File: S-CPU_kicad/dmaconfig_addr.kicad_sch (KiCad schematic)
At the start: 116 parts

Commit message: Big update on the hierarchical sheet. DMA section update too.
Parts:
- removed OCLC, OCLX: DFFR_A, symbol Ricoh_Cells:DFFR_A
- removed OMRS: INVERTER_A, symbol Ricoh_Cells:INVERTER_A
- removed ZOOJ: DFFR_B, symbol Ricoh_Cells:DFFR_B
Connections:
- net BUS_DIRECTION_FLAG: now reaches QKAG6.4 (Q)
- net wQKAG5 renamed INDIRECT_HDMA_FLAG
- net wWOVT renamed CYCLE_COUNTER0
- net wWOWE renamed CYCLE_COUNTER1
- no-connect marks 13 -> 9
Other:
- note removed: "DMA RW signal based on bus direction"
- moved on the sheet: DSAC, DSAZ, DSCS, DSKP, DSLL, DSSG, DSSX, DSWN, DSXY, DSYT, DSZC, OKWN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

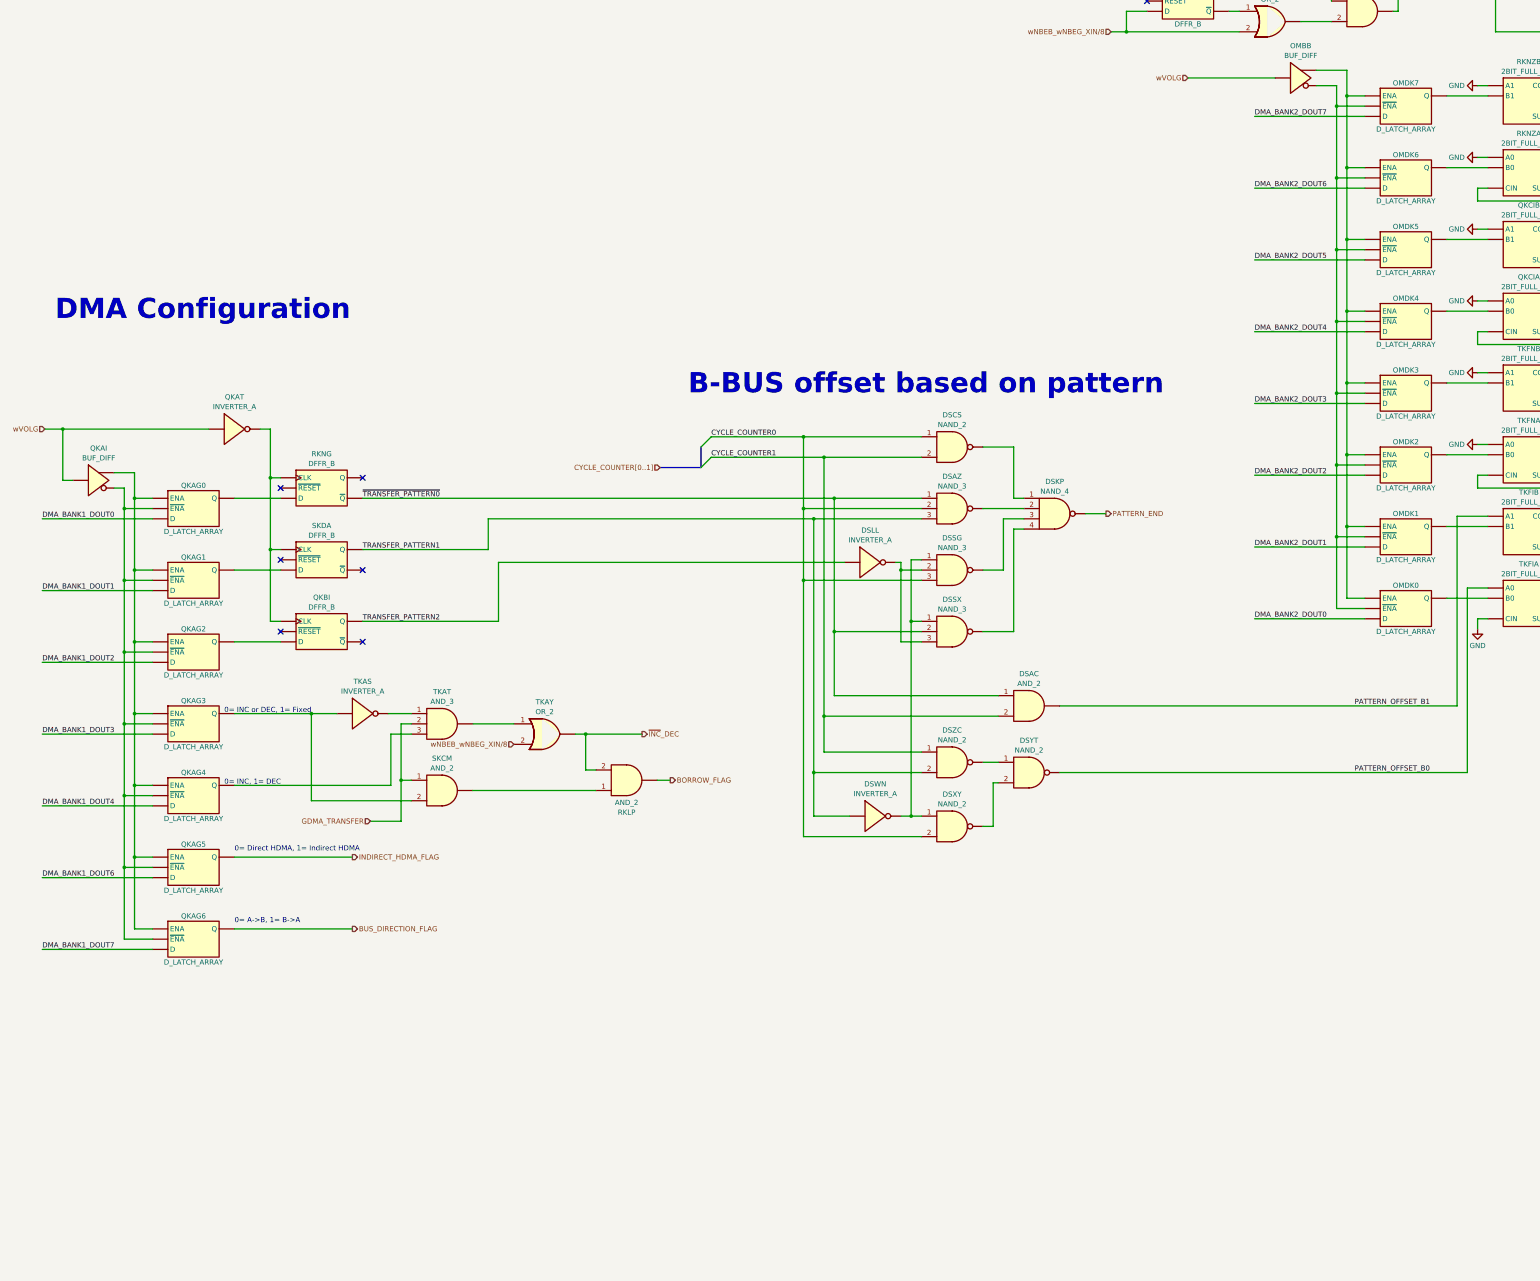
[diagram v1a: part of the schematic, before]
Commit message: DMA section update. Fixed gate related to INC/DEC and BORROW/CARRY FLAG
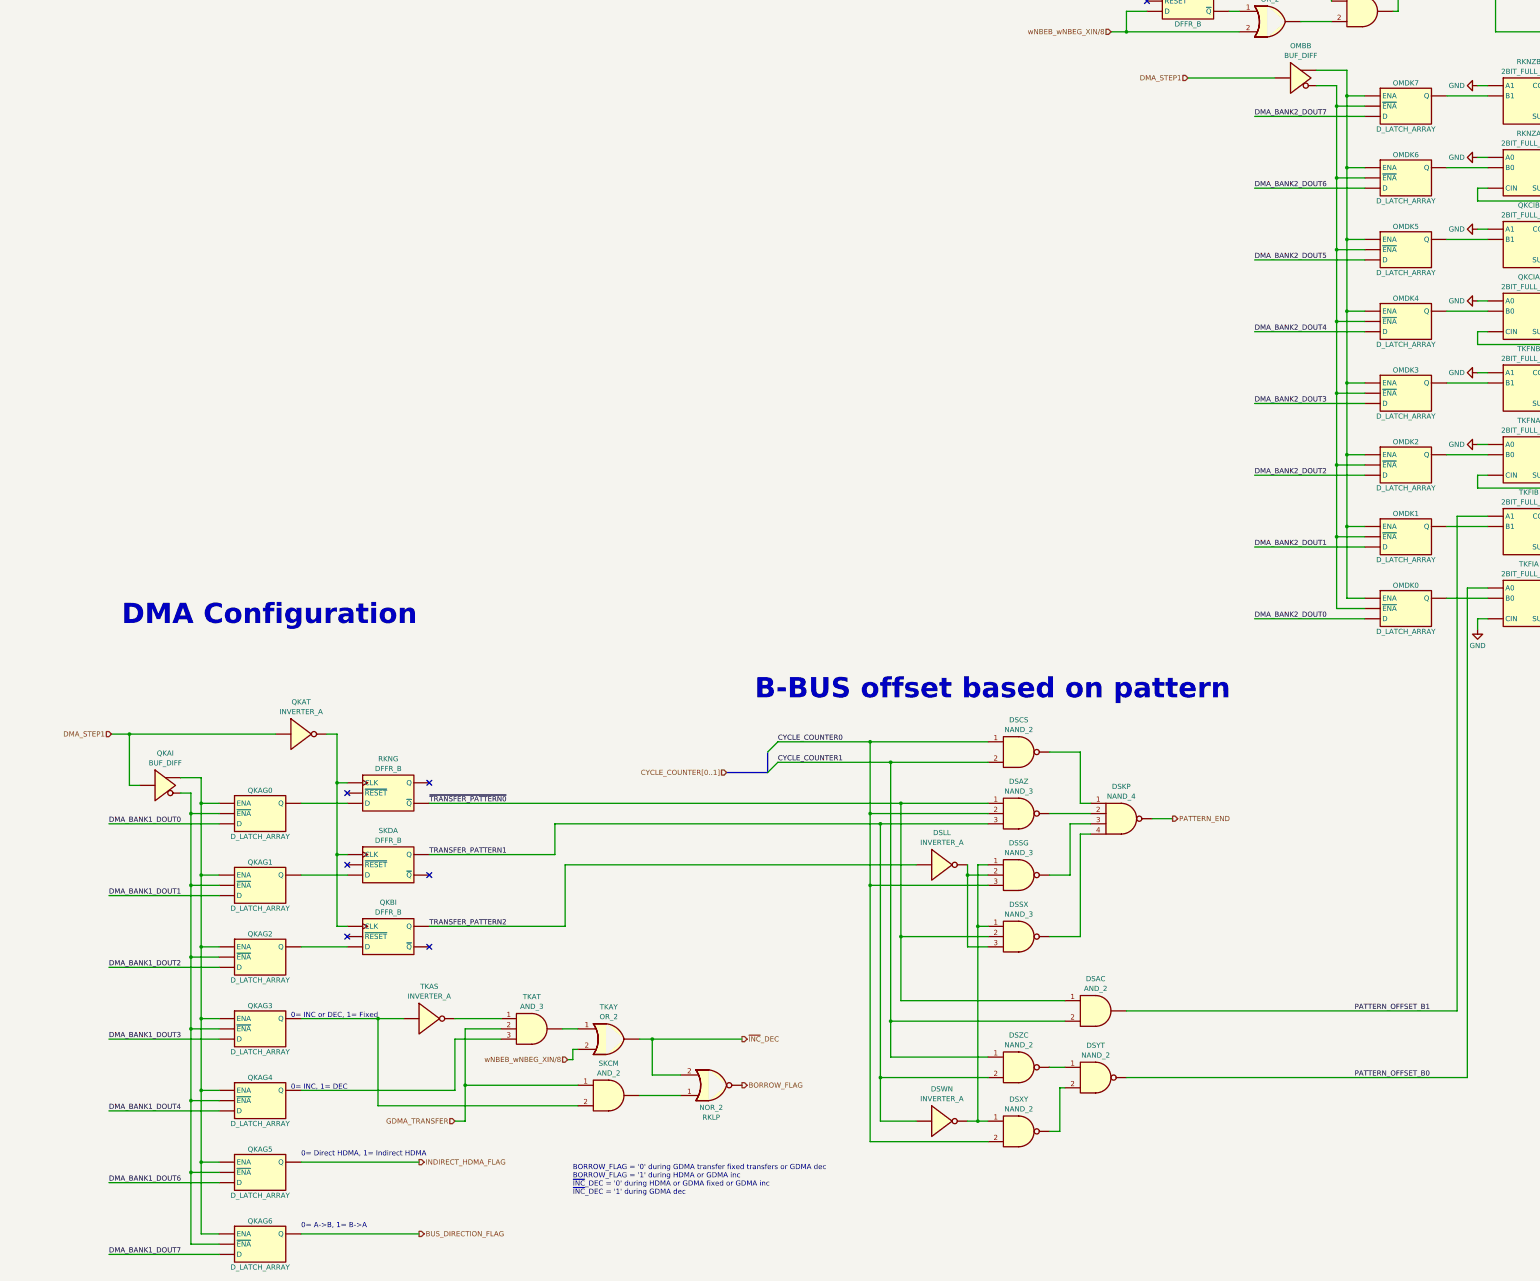
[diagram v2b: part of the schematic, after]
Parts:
- RKLP: value AND_2 -> NOR_2; symbol Ricoh_Cells:AND_2 -> Ricoh_Cells:NOR_2
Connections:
- net wVOLG renamed DMA_STEP1
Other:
- note added: "BORROW_FLAG = '0' during GDMA transfer fixed transfers or GDMA dec BORROW_FLAG = '1' during HDMA or GDMA inc ~{INC}_DEC = '0' during HDMA or GDMA fixed or GDMA inc ~{INC}_DEC = '1' during GDMA dec"
- moved on the sheet: DSAC, DSAZ, DSCS, DSKP, DSLL, DSSG, DSSX, DSWN, DSXY, DSYT, DSZC, QKAG0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

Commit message: DMA section update. Found errors between some MUX and MUXI gates.
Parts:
- TKHG: symbol Ricoh_Cells:OR_2 -> Ricoh_Cells:NOR_2
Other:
- note added: "LATCH_NEXT_DMA_ADDR_BUS is only valid for 1 mclk cycle every 8 cycles"
- note added: "Positive pulse on falling edge"
- moved on the sheet: SKKT, SKPA, TKGB, TKIB

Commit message: General update a
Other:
- note added: "LATCH_NEXT_DMA_ADDR_BUS is only valid for 1 mclk cycle every 8 cycles (on cycle 1)"
- note removed: "LATCH_NEXT_DMA_ADDR_BUS is only valid for 1 mclk cycle every 8 cycles"
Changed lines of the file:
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@@
     (effects (font (size 1.27 1.27)) (justify left bottom))
   )
-  (text "LATCH_NEXT_DMA_ADDR_BUS is only valid for 1 mclk cycle every 8 cycles"
+  (text "LATCH_NEXT_DMA_ADDR_BUS is only valid for 1 mclk cycle every 8 cycles (on cycle 1)"
     (at 425.45 57.15 0)
     (effects (font (size 1.27 1.27)) (justify left bottom))

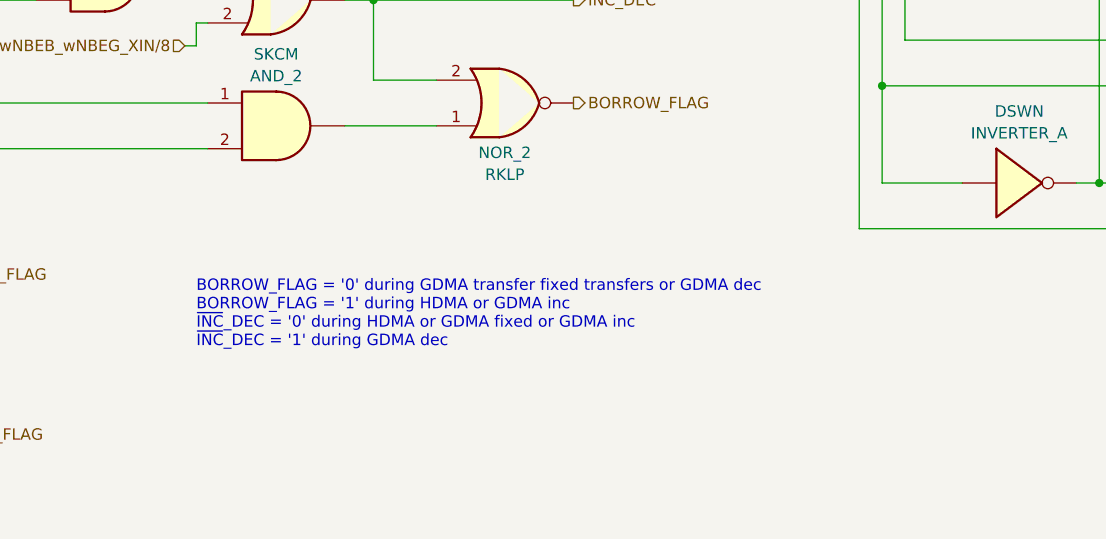
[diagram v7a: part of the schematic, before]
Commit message: More DMA updates - extra notes regarding behaviour
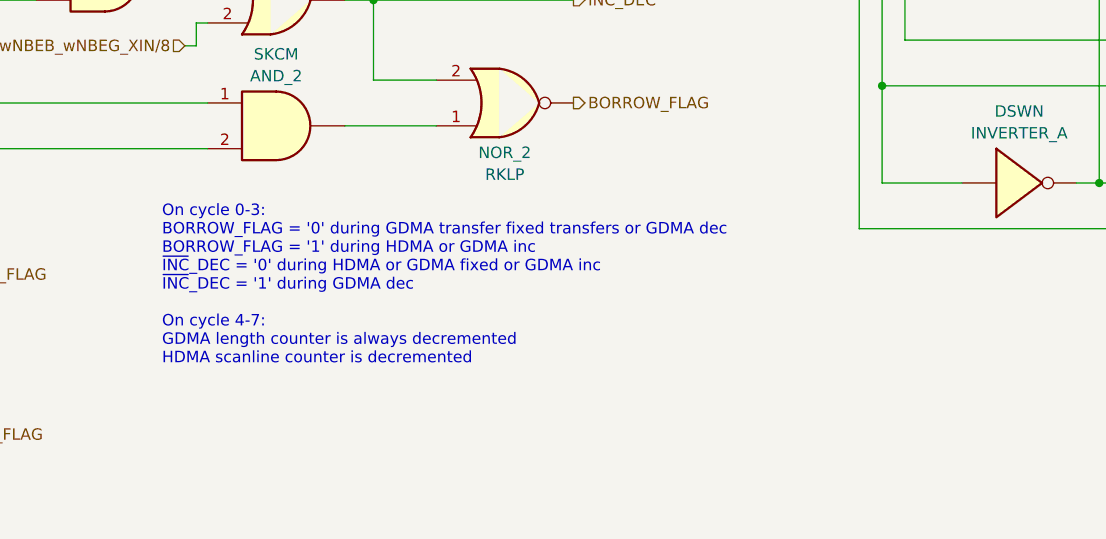
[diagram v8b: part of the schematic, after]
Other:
- note added: "On cycle 0-3: BORROW_FLAG = '0' during GDMA transfer fixed transfers or GDMA dec BORROW_FLAG = '1' during HDMA or GDMA inc ~{INC}_DEC = '0' during HDMA or GDMA fixed or GDMA inc ~{INC}_DEC = '1' during GDMA dec On cycle 4-7: GDMA length counter is always decremented HDMA scanline counter is decremented"
- note removed: "BORROW_FLAG = '0' during GDMA transfer fixed transfers or GDMA dec BORROW_FLAG = '1' during HDMA or GDMA inc ~{INC}_DEC = '0' during HDMA or GDMA fixed or GDMA inc ~{INC}_DEC = '1' during GDMA dec"
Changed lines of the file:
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@@
     (effects (font (size 5 5) (thickness 1) bold) (justify left bottom))
   )
-  (text "BORROW_FLAG = '0' during GDMA transfer fixed transfers or GDMA dec\nBORROW_FLAG = '1' during HDMA or GDMA inc\n~{INC}_DEC = '0' during HDMA or GDMA fixed or GDMA inc\n~{INC}_DEC = '1' during GDMA dec"
-    (at 187.96 380.365 0)
+  (text "On cycle 0-3:\nBORROW_FLAG = '0' during GDMA transfer fixed transfers or GDMA dec\nBORROW_FLAG = '1' during HDMA or GDMA inc\n~{INC}_DEC = '0' during HDMA or GDMA fixed or GDMA inc\n~{INC}_DEC = '1' during GDMA dec\n\nOn cycle 4-7:\nGDMA length counter is always decremented\nHDMA scanline counter is decremented "
+    (at 184.15 382.27 0)
     (effects (font (size 1.27 1.27)) (justify left bottom))
   )
